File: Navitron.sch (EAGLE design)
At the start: 92 parts, among them J2 DX07S016JA1R1500, Q1 ROHM_RUM002N02T2LROHM_RUM002N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, Q2 2.5A/30V, Q3 ROHM_RUM002N02T2LROHM_RUM002N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, Q4 ROHM_RUM002N02T2LROHM_RUM002N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, Q5 ROHM_RUM002N02T2LROHM_RUM002N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, T1 BC847, T2 BC847, U3 MCP73831, U5 CH340C

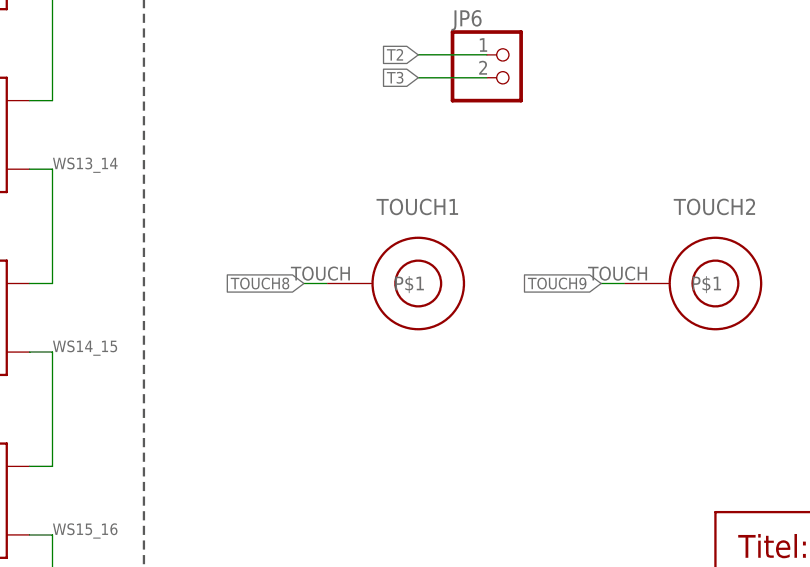
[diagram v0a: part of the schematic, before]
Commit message: Connect Touch Pad 8 & 9 and DRC Check
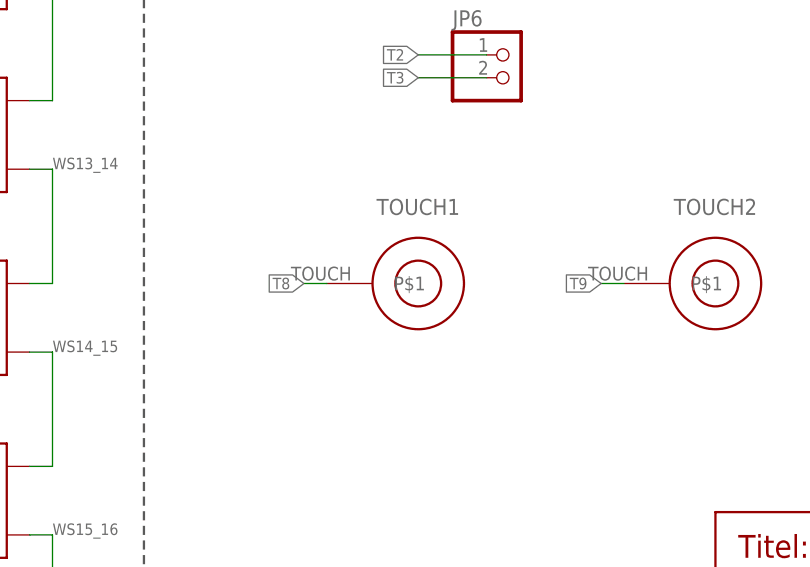
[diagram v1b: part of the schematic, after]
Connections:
- removed net TOUCH8: TOUCH1.P$1
- removed net TOUCH9: TOUCH2.P$1
- net T8: now also TOUCH1.P$1
- net T9: now also TOUCH2.P$1
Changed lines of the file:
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@@
-</segment>
-</net>
-<net name="TOUCH8" class="0">
-<segment>
-<wire x1="127" y1="-175.26" x2="124.46" y2="-175.26" width="0.1524" layer="91"/>
-<label x="124.46" y="-175.26" size="1.27" layer="95" rot="MR0" xref="yes"/>
-<pinref part="TOUCH1" gate="G$1" pin="P$1"/>
-</segment>
-</net>
-<net name="TOUCH9" class="0">
-<segment>
-<wire x1="160.02" y1="-175.26" x2="157.48" y2="-175.26" width="0.1524" layer="91"/>
-<label x="157.48" y="-175.26" size="1.27" layer="95" rot="MR0" xref="yes"/>
-<pinref part="TOUCH2" gate="G$1" pin="P$1"/>
 </segment>
 </net>
@@
 <label x="66.04" y="109.22" size="1.27" layer="95" xref="yes"/>
 </segment>
+<segment>
+<wire x1="127" y1="-175.26" x2="124.46" y2="-175.26" width="0.1524" layer="91"/>
+<label x="124.46" y="-175.26" size="1.27" layer="95" rot="MR0" xref="yes"/>
+<pinref part="TOUCH1" gate="G$1" pin="P$1"/>
+</segment>
 </net>
 <net name="T9" class="0">
@@
 <label x="66.04" y="106.68" size="1.27" layer="95" xref="yes"/>
 </segment>
+<segment>
+<wire x1="160.02" y1="-175.26" x2="157.48" y2="-175.26" width="0.1524" layer="91"/>
+<label x="157.48" y="-175.26" size="1.27" layer="95" rot="MR0" xref="yes"/>
+<pinref part="TOUCH2" gate="G$1" pin="P$1"/>
+</segment>
 </net>

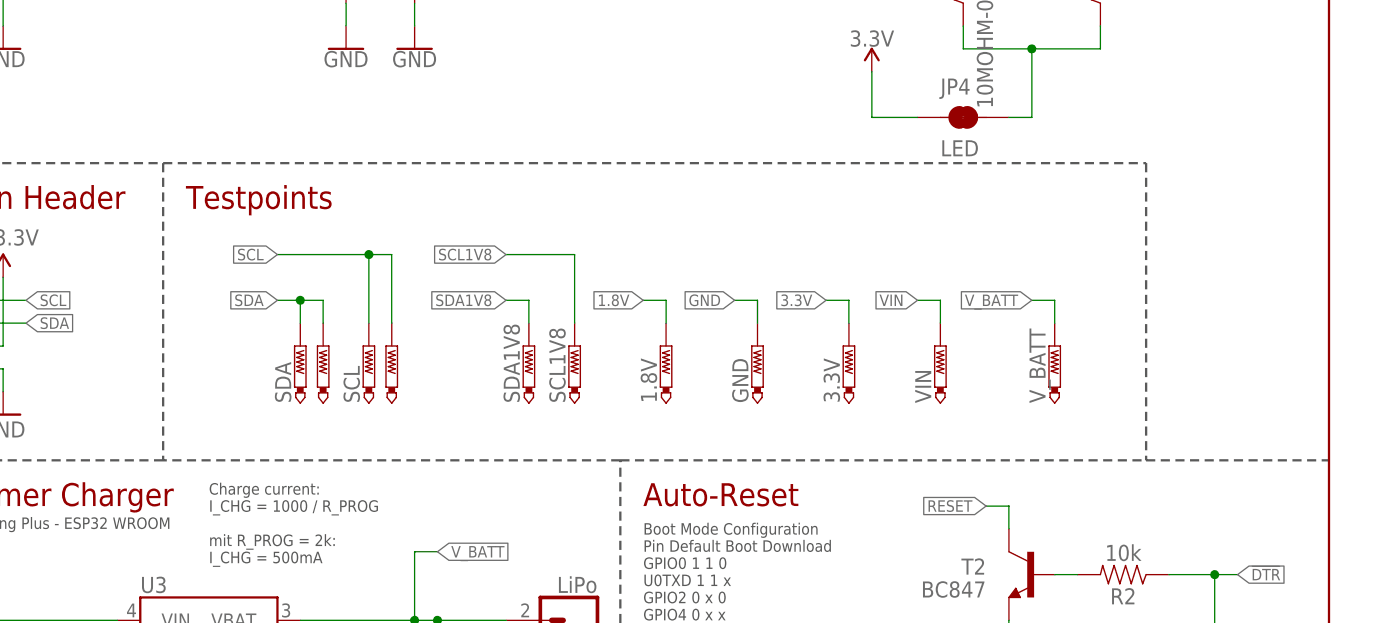
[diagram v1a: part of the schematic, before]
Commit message: Add Additional 1.8V SDA and SCL Pad
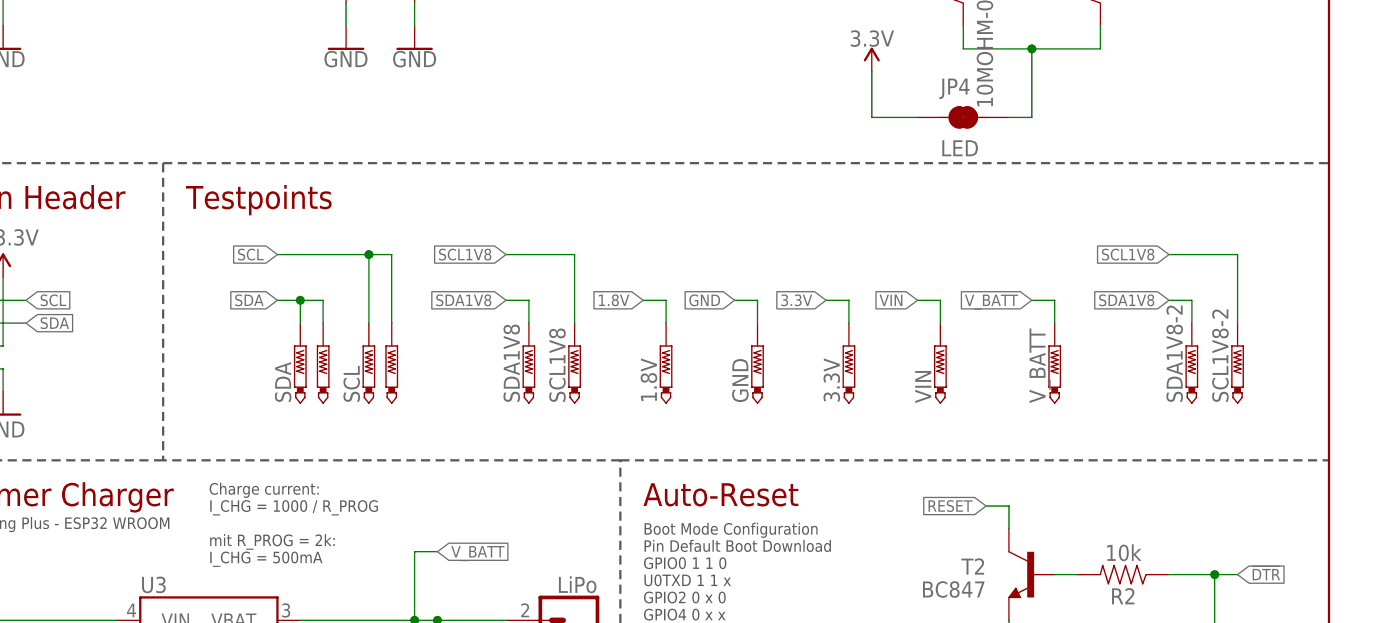
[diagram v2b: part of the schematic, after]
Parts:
- added SCL1V8-2, SDA1V8-2: PTR1B1,27, testpad:PTR1B1,27
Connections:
- net SCL1V8: now also SCL1V8-2.TP
- net SDA1V8: now also SDA1V8-2.TP
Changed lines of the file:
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@@
 <part name="TOUCH2" library="MyLib" deviceset="TOUCHPAD" device="8MM"/>
 <part name="JP6" library="pinhead" library_urn="urn:adsk.eagle:library:325" deviceset="PINHD-1X2" device="" package3d_urn="urn:adsk.eagle:package:22435/2"/>
+<part name="SDA1V8-2" library="testpad" library_urn="urn:adsk.eagle:library:385" deviceset="PTR1" device="B1,27" package3d_urn="urn:adsk.eagle:package:27944/2"/>
+<part name="SCL1V8-2" library="testpad" library_urn="urn:adsk.eagle:library:385" deviceset="PTR1" device="B1,27" package3d_urn="urn:adsk.eagle:package:27944/2"/>
 </parts>
 <sheets>
@@
 <wire x1="119.38" y1="76.2" x2="78.74" y2="76.2" width="0.254" layer="97" style="shortdash"/>
 <text x="81.28" y="106.68" size="2.54" layer="94" align="top-left">I2C Extension Header</text>
-<wire x1="170.18" y1="76.2" x2="228.6" y2="76.2" width="0.254" layer="97" style="shortdash"/>
-<wire x1="228.6" y1="76.2" x2="248.92" y2="76.2" width="0.254" layer="97" style="shortdash"/>
+<wire x1="170.18" y1="76.2" x2="248.92" y2="76.2" width="0.254" layer="97" style="shortdash"/>
 <wire x1="78.74" y1="109.22" x2="119.38" y2="109.22" width="0.254" layer="97" style="shortdash"/>
 <wire x1="119.38" y1="109.22" x2="119.38" y2="76.2" width="0.254" layer="97" style="shortdash"/>
@@
 <text x="190.5" y="-93.98" size="2.54" layer="94" align="top-left">Interrupt Level Shifting</text>
 <wire x1="187.96" y1="-137.16" x2="187.96" y2="-200.66" width="0.254" layer="97" style="shortdash"/>
-<wire x1="119.38" y1="109.22" x2="228.6" y2="109.22" width="0.254" layer="97" style="shortdash"/>
+<wire x1="119.38" y1="109.22" x2="248.92" y2="109.22" width="0.254" layer="97" style="shortdash"/>
 <text x="121.92" y="106.68" size="2.54" layer="94" align="top-left">Testpoints</text>
-<wire x1="228.6" y1="109.22" x2="228.6" y2="76.2" width="0.254" layer="97" style="shortdash"/>
 </plain>
 <instances>
@@
 <attribute name="NAME" x="140.97" y="-146.685" size="1.778" layer="95"/>
 <attribute name="VALUE" x="140.97" y="-157.48" size="1.778" layer="96"/>
+</instance>
+<instance part="SDA1V8-2" gate="G$1" x="233.68" y="88.9" smashed="yes">
+<attribute name="NAME" x="232.664" y="82.55" size="1.778" layer="95" rot="R90"/>
+<attribute name="TP_SIGNAL_NAME" x="234.95" y="86.36" size="1.778" layer="97"/>
+</instance>
+<instance part="SCL1V8-2" gate="G$1" x="238.76" y="88.9" smashed="yes">
+<attribute name="NAME" x="237.744" y="82.55" size="1.778" layer="95" rot="R90"/>
+<attribute name="TP_SIGNAL_NAME" x="240.03" y="86.36" size="1.778" layer="97"/>
 </instance>
 </instances>
@@
 <label x="157.48" y="93.98" size="1.27" layer="95" rot="MR0" xref="yes"/>
 </segment>
+<segment>
+<pinref part="SDA1V8-2" gate="G$1" pin="TP"/>
+<wire x1="233.68" y1="91.44" x2="233.68" y2="93.98" width="0.1524" layer="91"/>
+<wire x1="233.68" y1="93.98" x2="231.14" y2="93.98" width="0.1524" layer="91"/>
+<label x="231.14" y="93.98" size="1.27" layer="95" rot="MR0" xref="yes"/>
+</segment>
 </net>
 <net name="SCL1V8" class="0">
@@
 <label x="157.48" y="99.06" size="1.27" layer="95" rot="MR0" xref="yes"/>
 </segment>
-</net>
+<segment>
+<pinref part="SCL1V8-2" gate="G$1" pin="TP"/>
+<wire x1="238.76" y1="91.44" x2="238.76" y2="99.06" width="0.1524" layer="91"/>
+<wire x1="238.76" y1="99.06" x2="231.14" y2="99.06" width="0.1524" layer="91"/>
+<label x="231.14" y="99.06" size="1.27" layer="95" rot="MR0" xref="yes"/>
+</segment>
+</net>

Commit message: Small changes
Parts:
- CHARGING: value RED -> GREEN
- RX1, TX1: value YELLOW -> BLUE
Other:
- note added: "DMG2307"
- note added: "Testpads"
- note added: "Touch Pins"
- note removed: "Testpoints"
- moved on the sheet: JP6, TOUCH1, TOUCH2
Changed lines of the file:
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@@
 <part name="C8" library="SparkFun-Capacitors" deviceset="0.1UF" device="-0603-25V-(+80/-20%)" value="4.7uF"/>
 <part name="JP1" library="SparkFun-Connectors" deviceset="CONN_02" device="-JST-2MM-SMT" value="LiPo"/>
-<part name="CHARGING" library="SparkFun-LED" deviceset="LED-RED" device="0603" value="RED"/>
+<part name="CHARGING" library="SparkFun-LED" deviceset="LED-RED" device="0603" value="GREEN"/>
 <part name="SUPPLY8" library="SparkFun-PowerSymbols" deviceset="V_USB" device=""/>
 <part name="C7" library="SparkFun-Capacitors" deviceset="0.1UF" device="-0603-25V-(+80/-20%)" value="1.0uF"/>
@@
 <part name="SUPPLY16" library="SparkFun-PowerSymbols" deviceset="3.3V" device=""/>
 <part name="SUPPLY21" library="SparkFun-PowerSymbols" deviceset="3.3V" device=""/>
-<part name="RX1" library="SparkFun-LED" deviceset="LED-RED" device="0603" value="YELLOW"/>
-<part name="TX1" library="SparkFun-LED" deviceset="LED-RED" device="0603" value="YELLOW"/>
+<part name="RX1" library="SparkFun-LED" deviceset="LED-RED" device="0603" value="BLUE"/>
+<part name="TX1" library="SparkFun-LED" deviceset="LED-RED" device="0603" value="BLUE"/>
 <part name="R9" library="SparkFun-Resistors" deviceset="10MOHM" device="-0603-1/10W-5%" value="10MOHM-0603-1/10W-5%"/>
 <part name="R18" library="SparkFun-Resistors" deviceset="10MOHM" device="-0603-1/10W-5%" value="1k"/>
@@
 <text x="2.54" y="-48.26" size="2.54" layer="94" rot="MR270" align="top-left">LED Ring</text>
 <wire x1="106.68" y1="-91.44" x2="106.68" y2="-137.16" width="0.254" layer="97" style="shortdash"/>
-<wire x1="106.68" y1="-137.16" x2="106.68" y2="-231.14" width="0.254" layer="97" style="shortdash"/>
+<wire x1="106.68" y1="-137.16" x2="106.68" y2="-160.02" width="0.254" layer="97" style="shortdash"/>
+<wire x1="106.68" y1="-160.02" x2="106.68" y2="-231.14" width="0.254" layer="97" style="shortdash"/>
 <wire x1="106.68" y1="-91.44" x2="187.96" y2="-91.44" width="0.254" layer="97" style="shortdash"/>
 <wire x1="187.96" y1="-91.44" x2="187.96" y2="-45.72" width="0.254" layer="97" style="shortdash"/>
@@
 <text x="109.22" y="-55.88" size="1.27" layer="97">Orginal Mosfet: ROHM RE1C002UN</text>
 <text x="190.5" y="-93.98" size="2.54" layer="94" align="top-left">Interrupt Level Shifting</text>
-<wire x1="187.96" y1="-137.16" x2="187.96" y2="-200.66" width="0.254" layer="97" style="shortdash"/>
+<wire x1="187.96" y1="-137.16" x2="187.96" y2="-160.02" width="0.254" layer="97" style="shortdash"/>
+<wire x1="187.96" y1="-160.02" x2="187.96" y2="-200.66" width="0.254" layer="97" style="shortdash"/>
 <wire x1="119.38" y1="109.22" x2="248.92" y2="109.22" width="0.254" layer="97" style="shortdash"/>
-<text x="121.92" y="106.68" size="2.54" layer="94" align="top-left">Testpoints</text>
+<text x="121.92" y="106.68" size="2.54" layer="94" align="top-left">Testpads</text>
+<text x="109.22" y="-139.7" size="2.54" layer="94" align="top-left">Touch Pins</text>
+<wire x1="106.68" y1="-160.02" x2="187.96" y2="-160.02" width="0.254" layer="97" style="shortdash"/>
+<text x="53.34" y="30.48" size="1.778" layer="95">DMG2307</text>
 </plain>
 <instances>
@@
 <instance part="R9" gate="G$1" x="208.28" y="129.54" smashed="yes" rot="R90">
 <attribute name="NAME" x="206.756" y="129.54" size="1.778" layer="95" font="vector" rot="R90" align="bottom-center"/>
-<attribute name="VALUE" x="209.804" y="129.54" size="1.778" layer="96" font="vector" rot="R90" align="top-center"/>
 </instance>
 <instance part="R18" gate="G$1" x="223.52" y="129.54" smashed="yes" rot="R90">
@@
 <attribute name="VALUE" x="139.7" y="-124.714" size="1.778" layer="96" font="vector" align="top-left"/>
 </instance>
-<instance part="TOUCH1" gate="G$1" x="137.16" y="-175.26" smashed="yes">
-<attribute name="NAME" x="137.16" y="-167.64" size="1.778" layer="95" align="bottom-center"/>
-</instance>
-<instance part="TOUCH2" gate="G$1" x="170.18" y="-175.26" smashed="yes">
-<attribute name="NAME" x="170.18" y="-167.64" size="1.778" layer="95" align="bottom-center"/>
-</instance>
-<instance part="JP6" gate="G$1" x="147.32" y="-152.4" smashed="yes">
-<attribute name="NAME" x="140.97" y="-146.685" size="1.778" layer="95"/>
-<attribute name="VALUE" x="140.97" y="-157.48" size="1.778" layer="96"/>
+<instance part="TOUCH1" gate="G$1" x="147.32" y="-149.86" smashed="yes">
+<attribute name="NAME" x="147.32" y="-142.24" size="1.778" layer="95" align="bottom-center"/>
+</instance>
+<instance part="TOUCH2" gate="G$1" x="175.26" y="-149.86" smashed="yes">
+<attribute name="NAME" x="175.26" y="-142.24" size="1.778" layer="95" align="bottom-center"/>
+</instance>
+<instance part="JP6" gate="G$1" x="124.46" y="-152.4" smashed="yes">
+<attribute name="NAME" x="118.11" y="-146.685" size="1.778" layer="95"/>
+<attribute name="VALUE" x="118.11" y="-157.48" size="1.778" layer="96"/>
 </instance>
 <instance part="SDA1V8-2" gate="G$1" x="233.68" y="88.9" smashed="yes">
@@
 <segment>
 <pinref part="JP6" gate="G$1" pin="1"/>
-<wire x1="144.78" y1="-149.86" x2="137.16" y2="-149.86" width="0.1524" layer="91"/>
-<label x="137.16" y="-149.86" size="1.27" layer="95" rot="MR0" xref="yes"/>
+<wire x1="121.92" y1="-149.86" x2="114.3" y2="-149.86" width="0.1524" layer="91"/>
+<label x="114.3" y="-149.86" size="1.27" layer="95" rot="MR0" xref="yes"/>
 </segment>
 </net>
@@
 <segment>
 <pinref part="JP6" gate="G$1" pin="2"/>
-<wire x1="144.78" y1="-152.4" x2="137.16" y2="-152.4" width="0.1524" layer="91"/>
-<label x="137.16" y="-152.4" size="1.27" layer="95" rot="MR0" xref="yes"/>
+<wire x1="121.92" y1="-152.4" x2="114.3" y2="-152.4" width="0.1524" layer="91"/>
+<label x="114.3" y="-152.4" size="1.27" layer="95" rot="MR0" xref="yes"/>
 </segment>
 </net>
@@
 </segment>
 <segment>
-<wire x1="127" y1="-175.26" x2="124.46" y2="-175.26" width="0.1524" layer="91"/>
-<label x="124.46" y="-175.26" size="1.27" layer="95" rot="MR0" xref="yes"/>
+<wire x1="137.16" y1="-149.86" x2="134.62" y2="-149.86" width="0.1524" layer="91"/>
+<label x="134.62" y="-149.86" size="1.27" layer="95" rot="MR0" xref="yes"/>
 <pinref part="TOUCH1" gate="G$1" pin="P$1"/>
 </segment>
@@
 </segment>
 <segment>
-<wire x1="160.02" y1="-175.26" x2="157.48" y2="-175.26" width="0.1524" layer="91"/>
-<label x="157.48" y="-175.26" size="1.27" layer="95" rot="MR0" xref="yes"/>
+<wire x1="165.1" y1="-149.86" x2="162.56" y2="-149.86" width="0.1524" layer="91"/>
+<label x="162.56" y="-149.86" size="1.27" layer="95" rot="MR0" xref="yes"/>
 <pinref part="TOUCH2" gate="G$1" pin="P$1"/>
 </segment>

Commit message: Change Revision Number
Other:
- note added: "v2"
- note removed: "v1"
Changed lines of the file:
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@@
 <wire x1="223.52" y1="7.62" x2="223.52" y2="15.24" width="0.254" layer="94"/>
 <text x="226.06" y="10.16" size="2.54" layer="94">Rev:</text>
-<text x="246.38" y="10.16" size="2.54" layer="94" rot="MR0">v1</text>
+<text x="246.38" y="10.16" size="2.54" layer="94" rot="MR0">v2</text>
 <wire x1="170.18" y1="15.24" x2="170.18" y2="22.86" width="0.254" layer="94"/>
 <wire x1="170.18" y1="22.86" x2="248.92" y2="22.86" width="0.254" layer="94"/>
@@
 <wire x1="223.52" y1="-223.52" x2="223.52" y2="-215.9" width="0.254" layer="94"/>
 <text x="226.06" y="-220.98" size="2.54" layer="94">Rev:</text>
-<text x="246.38" y="-220.98" size="2.54" layer="94" rot="MR0">v1</text>
+<text x="246.38" y="-220.98" size="2.54" layer="94" rot="MR0">v2</text>
 <wire x1="170.18" y1="-215.9" x2="170.18" y2="-208.28" width="0.254" layer="94"/>
 <wire x1="170.18" y1="-208.28" x2="248.92" y2="-208.28" width="0.254" layer="94"/>
